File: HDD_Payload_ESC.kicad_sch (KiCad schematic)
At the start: 27 parts, among them J1 Conn_01x05_Pin, J2 Conn_01x03_Pin, J3 Conn_01x06_Pin, J4 Screw_Terminal_01x02, SW1 SW_Push, U1 STM32G431CBUx, U2 AP3402, Y1 Crystal_GND24

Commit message: labeling update
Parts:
- removed C11, C12: 10p, Capacitor_SMD:C_0402_1005Metric, symbol Device:C_Small
- removed C7: 1u, Capacitor_SMD:C_0402_1005Metric, symbol Device:C_Small
- removed C9: 22u, symbol Device:C_Small
- removed J4: Screw_Terminal_01x02, symbol Connector:Screw_Terminal_01x02
- removed R1: 100k, symbol Device:R_Small
- removed Y1: Crystal_GND24, symbol Device:Crystal_GND24
- added R4, R5, R6: 10k, symbol Device:R_Small
- added R7: 100k, symbol Device:R_Small
- L2: value L_Small -> 2.2u
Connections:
- net +5V: now also R7.2
- net PA10: now also R6.1; no longer D1.3 (BK)
- net PA8: now also R4.1; no longer D1.1 (RK)
- net PA9: now also R5.1; no longer D1.2 (GK)
- net at U1.16 (PC4): now also J3.1 (Pin_1)
- net at U1.2 (PC13): now also J3.5 (Pin_5)
- net at U1.29 (PC6): now also J3.2 (Pin_2)
- net at U1.3 (PC14): now also J3.6 (Pin_6)
- net at U1.39 (PC10): now also J3.3 (Pin_3)
- net at U1.40 (PC11): now also J3.4 (Pin_4)
- net BUCK_OUT: no longer names the net of L2.1, U2.3 (LX)
- net FB: no longer names the net of R2.1, R3.2, U2.6 (FB)
- net HSE_IN: no longer names the net of U1.5 (PF0)
- net HSE_OUT: no longer names the net of U1.6 (PF1)
- net PA0 renamed Fets/PA0
- net PA1 renamed Fets/PA1
- net PA2 renamed Fets/PA2
- net PA3 renamed Fets/PA3
- net PA4 renamed Fets/PA4
- net PA5 renamed Fets/PA5
- net PB0: no longer names the net of U1.17 (PB0)
- net PB0: no longer J3.1 (Pin_1)
- net PB1: no longer names the net of U1.18 (PB1)
- net PB1: no longer J3.2 (Pin_2)
- net PB2: no longer names the net of U1.19 (PB2)
- net PB2: no longer J3.3 (Pin_3)
- net PB3: no longer names the net of U1.41 (PB3)
- net PB3: no longer J3.4 (Pin_4)
- net PB4: no longer names the net of U1.42 (PB4)
- net PB4: no longer J3.5 (Pin_5)
- net PB5: no longer names the net of U1.43 (PB5)
- net PB5: no longer J3.6 (Pin_6)
- net PG: no longer names the net of U2.5 (PG)
- net PG: now also R7.1
- net PIN_HEADER_1 renamed Fets/PIN_HEADER_1
- net PIN_HEADER_2 renamed Fets/PIN_HEADER_2
- net PIN_HEADER_3 renamed Fets/PIN_HEADER_3
- new net: D1.1 (RK), R4.2
- new net: D1.2 (GK), R5.2
- new net: D1.3 (BK), R6.2
- no-connect marks 22 -> 24
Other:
- sheet Fets ports: added PA0, PA1, PA2, PA3, PA4, PA5, PIN_HEADER_1, PIN_HEADER_2, PIN_HEADER_3; removed none
- note added: "GPIOC"
- note removed: "GPIOB"
- moved on the sheet: C1, C10, C2, C3, C4, C5, C6, C8, D1, F1, J1, J2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

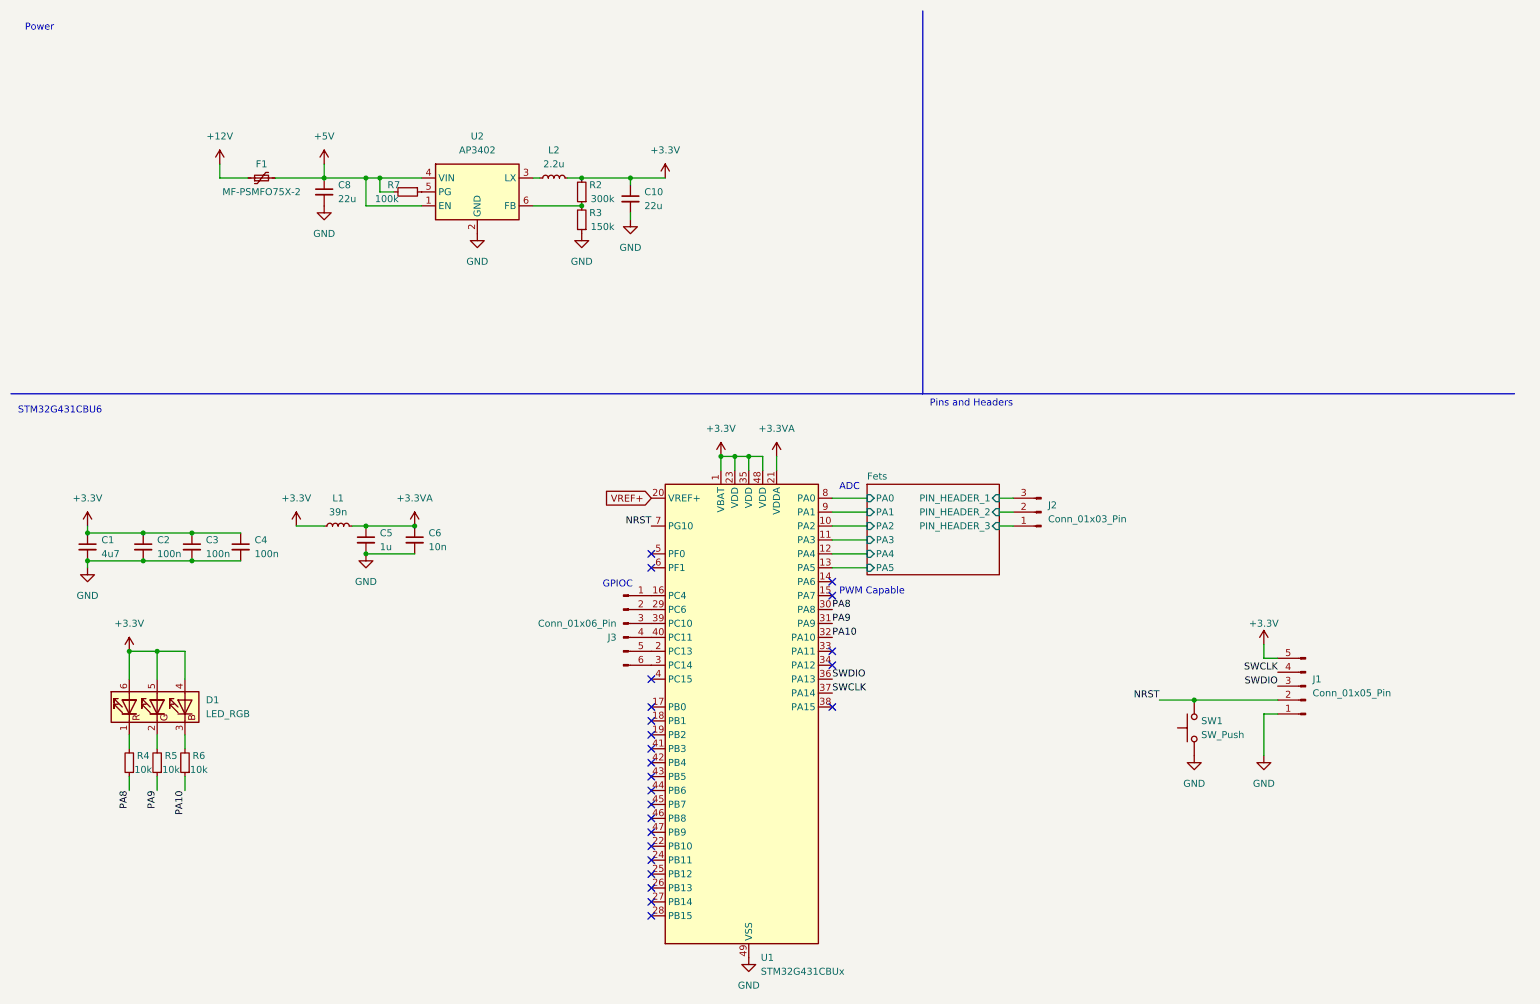
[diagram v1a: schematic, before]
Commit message: Gate To Fets added
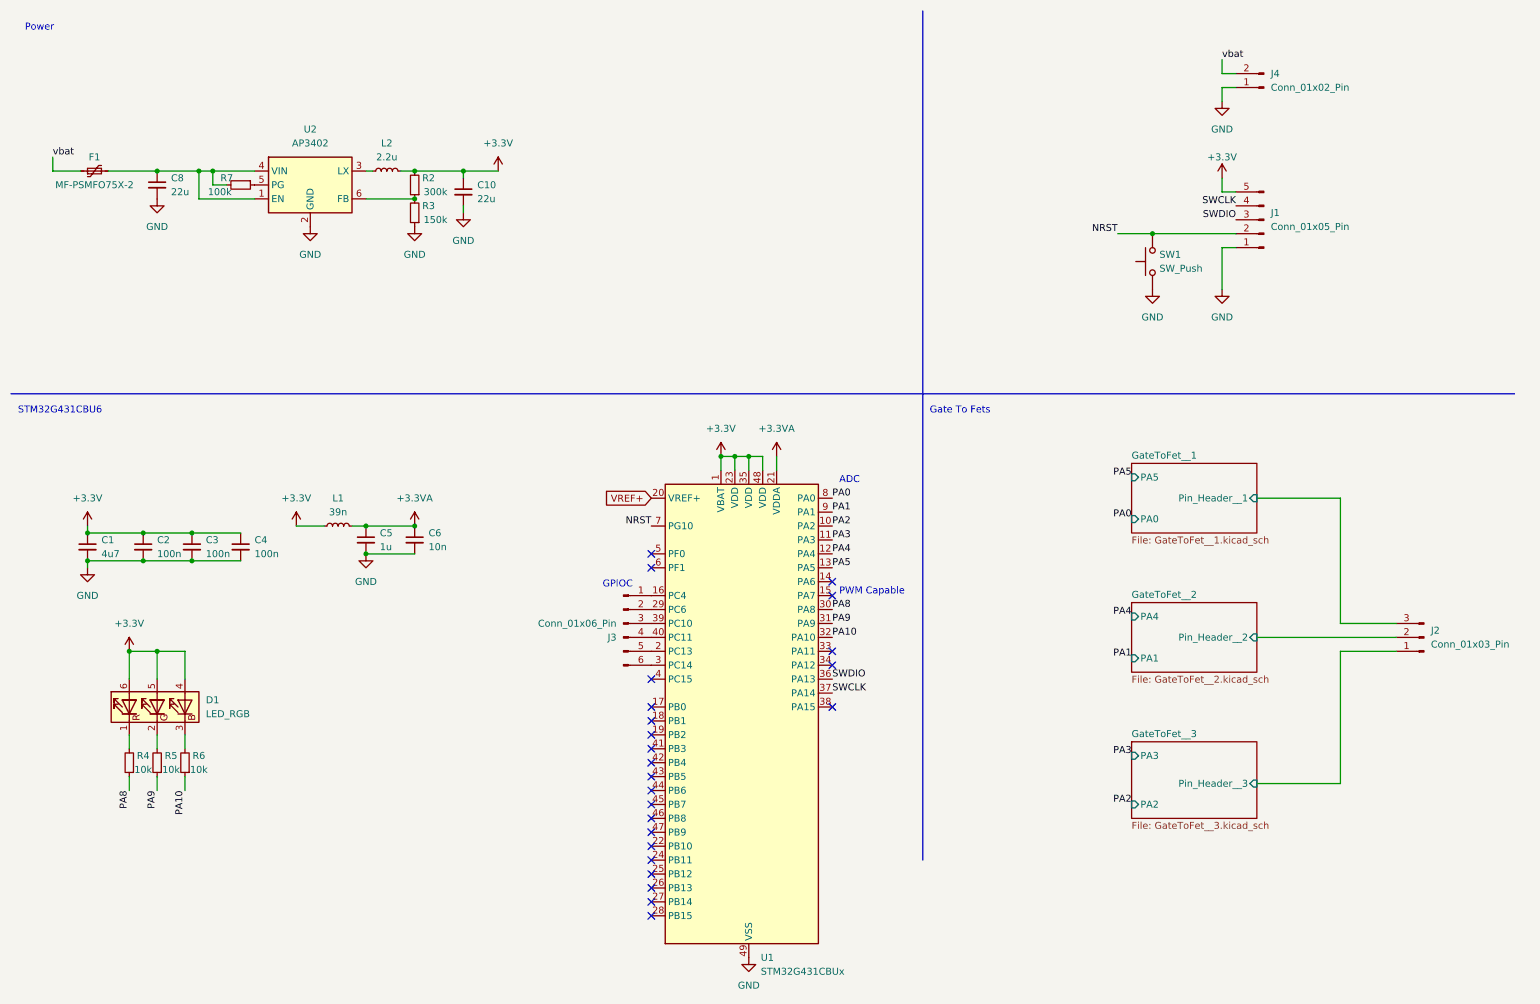
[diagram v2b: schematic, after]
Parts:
- added J4: Conn_01x02_Pin, symbol Connector:Conn_01x02_Pin
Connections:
- net GND: now also J4.1 (Pin_1)
- net +12V renamed vbat
- net vbat: now also J4.2 (Pin_2)
- net +5V: no longer names the net of C8.1, F1.2, R7.2, U2.1 (EN), U2.4 (VIN)
- net Fets/PA0 renamed PA0
- net Fets/PA1 renamed PA1
- net Fets/PA2 renamed PA2
- net Fets/PA3 renamed PA3
- net Fets/PA4 renamed PA4
- net Fets/PA5 renamed PA5
- net Fets/PIN_HEADER_1 renamed GateToFet__1/Pin_Header__1
- net Fets/PIN_HEADER_2 renamed GateToFet__2/Pin_Header__2
- net Fets/PIN_HEADER_3 renamed GateToFet__3/Pin_Header__3
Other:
- removed sheet Fets
- added sheet GateToFet__1 (GateToFet__1.kicad_sch)
- added sheet GateToFet__2 (GateToFet__2.kicad_sch)
- added sheet GateToFet__3 (GateToFet__3.kicad_sch)
- note added: "Gate To Fets"
- note removed: "Pins and Headers"
- moved on the sheet: C10, C8, F1, J1, J2, L2, R2, R3, R7, SW1, U2
